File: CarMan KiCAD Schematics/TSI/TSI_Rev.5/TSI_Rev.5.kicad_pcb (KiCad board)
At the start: 2 copper layers, 203.2 x 165.1 mm, 259 parts, among them IC1 TS431ILT, IC4 TS431ILT, J1 J1, J10 J10, J11 J11, J12 J12, J13 Conn_01x01, J13.1 Conn_01x06, J13.2 Conn_01x06, J14 J14, J15 J15, J16 J16, J17 J17, J18 J18, J19 J19, J2 Current_Sensor, J20 J20, J21 J21, J22 J22, J23 J23, J24 Conn_01x01, J25 Conn_01x01, J26 J26, J27 J27, J28 Conn_01x01, J29 J29, J3 J3, J30 J23, J4 J4, J5 J5, J6 J6, J7 J7, J8 J8, J9 J9, K1 APAN3105, K2 G5LE-1-E, K3 SFS2-DC24V, K4 SFS2-DC24V, Q1 ZVP1320F, Q11 TN2130K1-G, Q2 MMBF170, Q3 ZVP1320F, Q5 SI1302DL-T1-E3, SW1 TS5A3159DBVT, U1 RDE03110S12, U10 MC7805BDTRKG, U11 TLP293, U12 REF3033, U13 TLP293, U14 Bottom Left, U15 Top Left, U16 TS372CDT, U17 Top Right, U18 MCP6004, U19 74HC00, U2 Bottom Right, U20 TLP293, U21 MCP6004, U22 MCP23016-I_SO, U23 DAC5574IDGS, U24 TLP293, U25 NCD9830DBR2G, U26 MCP6004, U29 SN74LVC1G08DCKR, U3 TS912, U30 TLP293, U31 TLP293, U32 TLP293, U34 TLP293, U35 MCP6004, U37 TLP293, U4 ACPL-C870, U40 MCP6004, U41 PDQ10-Q24-D5-D, U42 LT1763CS8-3.3PBF, U48 TLP293, U49 TLP293, U5 SI8600AB-B-IS, U6 TS912, U7 MCP6004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

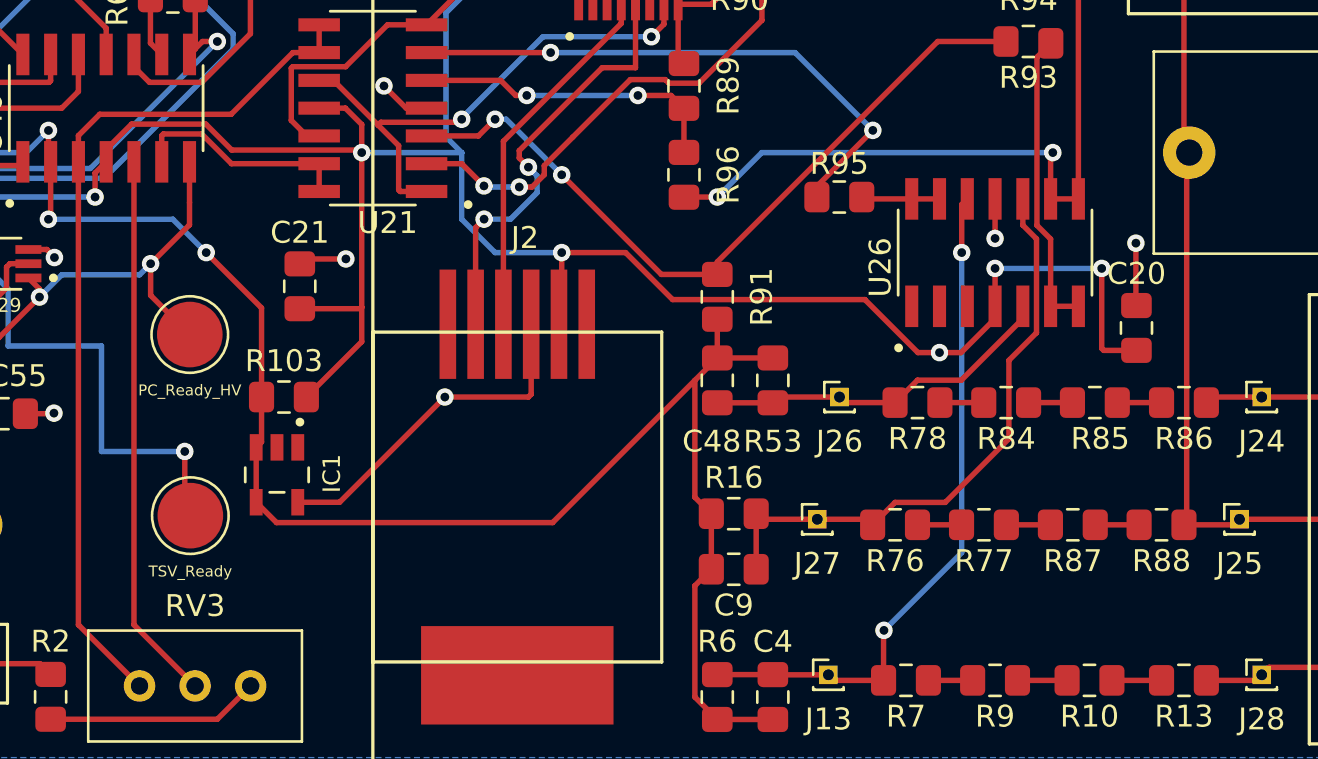
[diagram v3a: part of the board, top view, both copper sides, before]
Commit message: Contemplated homicide and fixed PC schematic
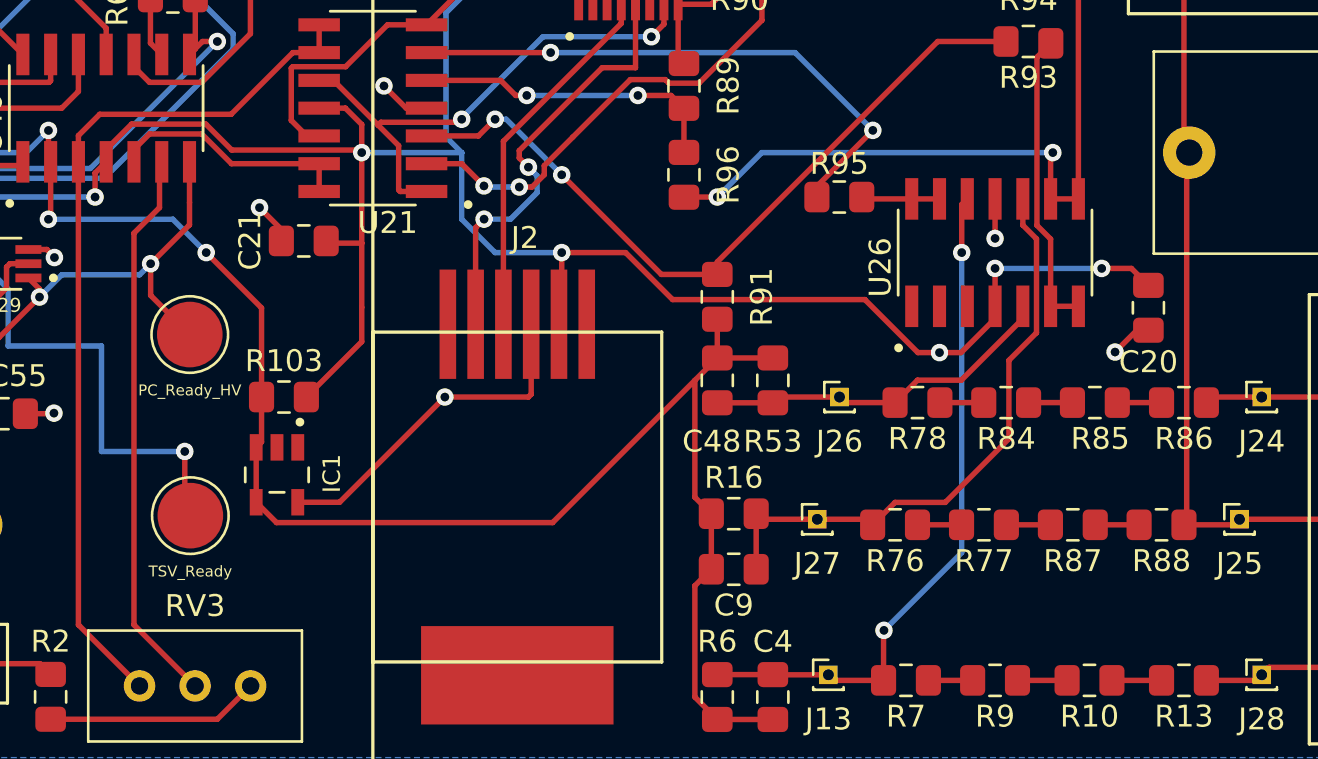
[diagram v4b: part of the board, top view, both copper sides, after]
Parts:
- moved C21 2.08 mm to (230.1, 194.1), turned to 180 degrees
- moved C20 1.07 mm to (268.7, 197.1), turned to 270 degrees
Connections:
- U40 pad 5: Net-(RV3-Pad2) -> Net-(U21-Pad13)
- U40 pad 6: Net-(U21-Pad13) -> Net-(RV3-Pad2)
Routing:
- net /5HV: track 312.8 -> 308.8 mm
- net /DC_RELAY-: track 100.9 -> 99.7 mm
- net Net-(U21-Pad13): track 10.3 -> 11.2 mm
- net Net-(RV3-Pad2): track 25.1 -> 25.6 mm

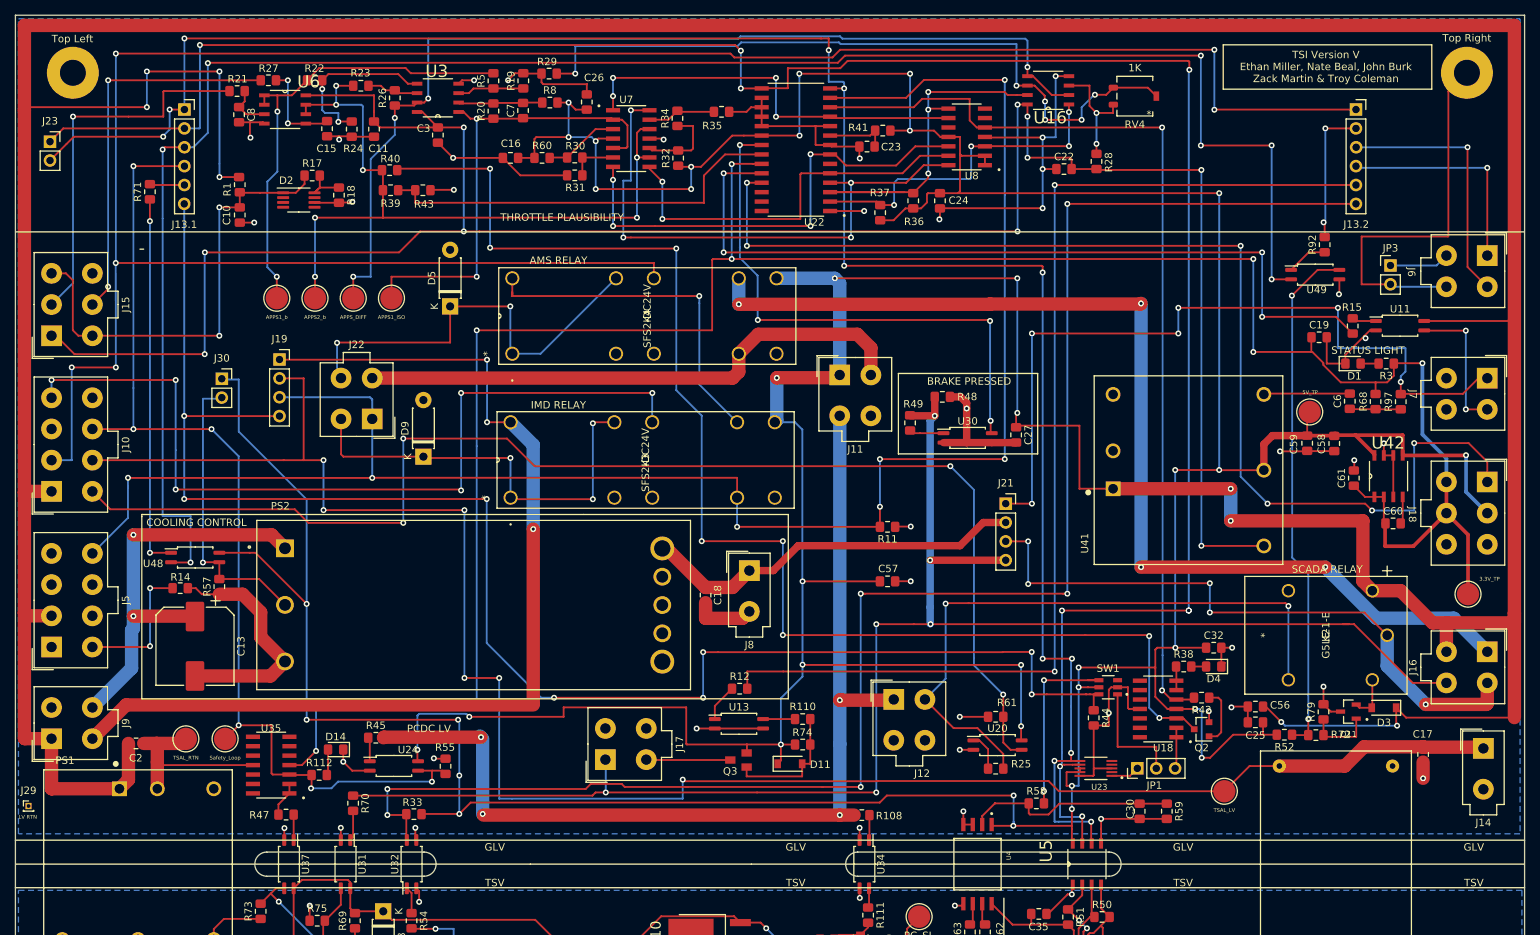
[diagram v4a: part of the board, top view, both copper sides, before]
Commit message: - Increased spacing between edge cuts and 24V - Labeled more in Low voltage
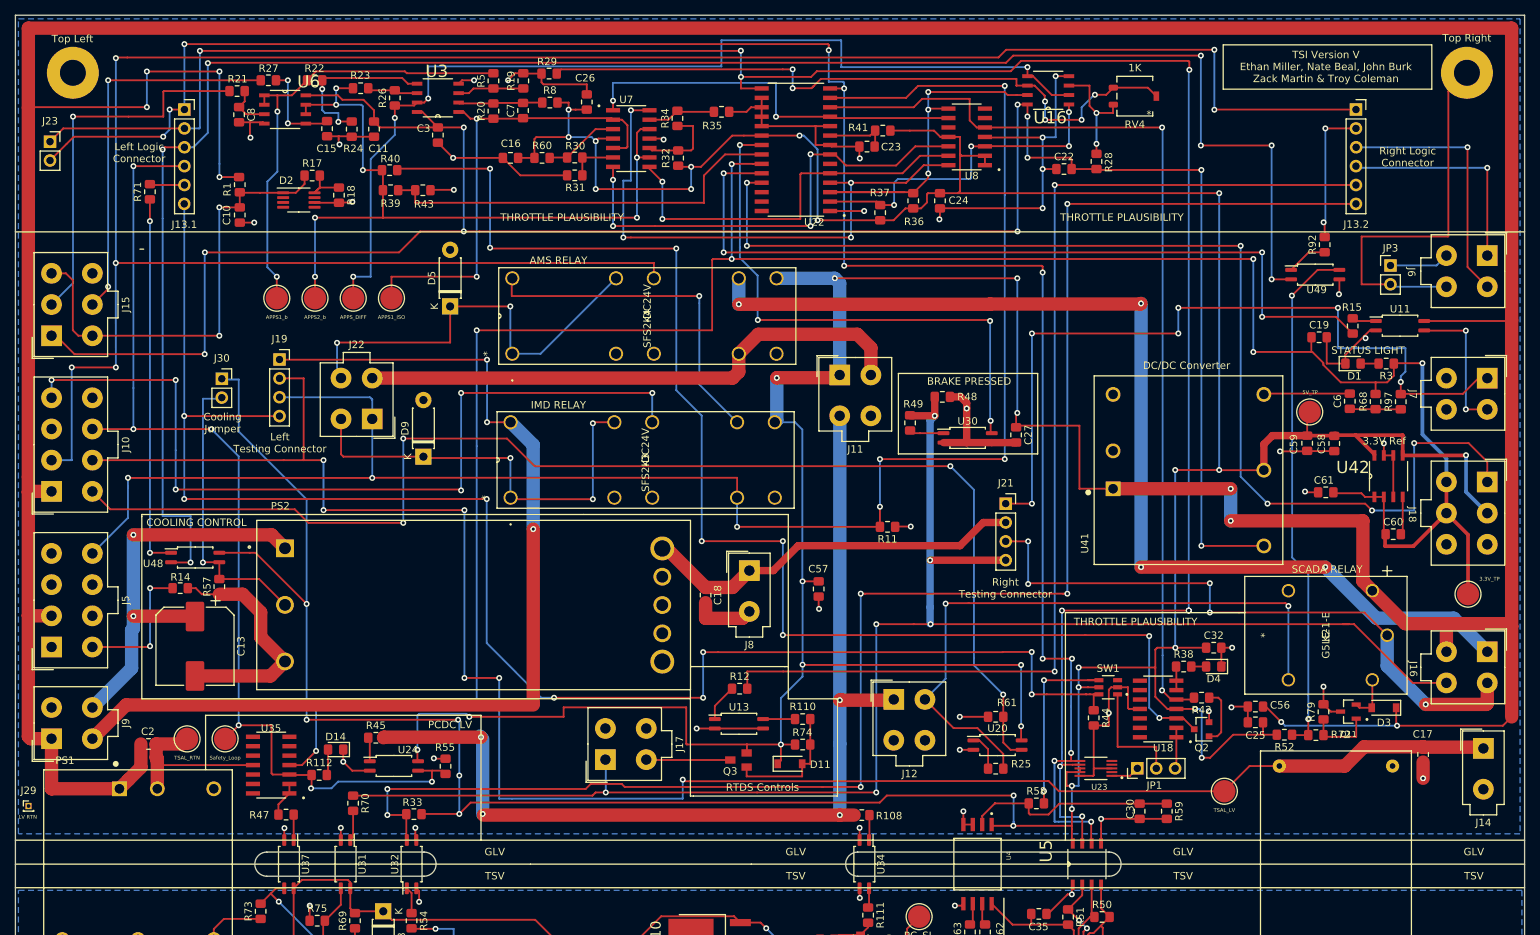
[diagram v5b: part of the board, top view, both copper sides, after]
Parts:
- moved C57 9.33 mm to (208.3, 130.1), turned to 270 degrees
- moved C61 4.24 mm to (276.6, 117.1), turned to 180 degrees
- moved C2 1.68 mm to (118.1, 151.0)
- moved C60 1.45 mm to (285.7, 122.7)
- moved R23 0.33 mm to (146.7, 62.7)
- moved TP14 0.17 mm to (123.3, 150.3)
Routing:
- net /24V: track 864.3 -> 850.7 mm
- net /5V: track 569.4 -> 559.3 mm, vias 28 -> 26
- net Net-(R29-Pad1): track 97.4 -> 92.2 mm
- net /3.3V: track 311.4 -> 313.8 mm
- net Net-(C60-Pad2): track 3.68 -> 5.28 mm
- net /SCL: track 270.3 -> 268.7 mm
- net /TSI-TP/U8_Pin9: track 54.8 -> 53.5 mm, vias 4 -> 2
- net /10V: track 298.4 -> 297.2 mm
- net /IMD_Status: track 245.1 -> 244.0 mm
- net /AIRS-: track 361.0 -> 360.0 mm
- net /AMS_FAULT_LED: track 313.5 -> 313.0 mm
- net /TSI-TP/APPS_DIFF: track 135.0 -> 134.5 mm
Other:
- board text added: "3.3V Ref"
- board text added: "Cooling Jumper"
- board text added: "DC/DC Converter"
- board text added: "J16"
- board text added: "Left Logic Connector"
- board text added: "Left Testing Connector"
- board text added: "RTDS Controls"
- board text added: "Right Logic Connector"
- board text added: "Right Testing Connector"

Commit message: TSI Silkscreen Connector Descriptions added
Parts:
- J1 HV: renamed from J1
- J10 DASH: renamed from J10
- J11 BP PWR: renamed from J11
- J12 MRST SLOOP: renamed from J12
- J13.1 Logic: renamed from J13.1
- J13.2 Logic: renamed from J13.2
- J14 TSAL: renamed from J14
- J15 Throt. Plaus.: renamed from J15
- J17 Light RTDS: renamed from J17
- J2 Current: renamed from J2
- J20 Discharge : renamed from J20
- J22 LSP: renamed from J22
- J23 I2C: renamed from J23
- J3 PC: renamed from J3
- J4 MC: renamed from J4
- J5 IMD: renamed from J5
- J8 COOL PWR: renamed from J8
- J9 GLV: renamed from J9
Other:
- board text added: "J16 Brake"
- board text added: "J18 COOL Sensor"
- board text added: "J6 BP CAN"
- board text added: "J7 Cockpit"
- board text removed: "J16"
- board text removed: "J18"
- board text removed: "J6"
- board text removed: "J7"

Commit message: TSI silkscreen updated
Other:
- board text added: "TSI Version V Nate Beal, Ethan Miller, John Burk Zack Martin & Troy Coleman"
- board text removed: "TSI Version V Ethan Miller, Nate Beal, John Burk Zack Martin & Troy Coleman"
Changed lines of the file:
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@@
   (general
     (thickness 1.6)
-    (drawings 89)
+    (drawings 88)
     (tracks 2617)
     (zones 0)
@@
     (descr "Molex Mini-Fit JR, PN:5556-04A, dual row, top entry type, through hole")
     (tags "connector molex mini-fit 5556")
-    (fp_text reference "J9 GLV" (at -0.2286 9.8933 90) (layer F.SilkS)
+    (fp_text reference "J9 GLV" (at 1.8288 10.1219 90) (layer F.SilkS)
       (effects (font (size 1 1) (thickness 0.15)))
     )
@@
     (descr "Molex Mini-Fit JR, PN:5556-08A, dual row, top entry type, through hole")
     (tags "connector molex mini-fit 5556")
-    (fp_text reference "J5 IMD" (at 7.747 10 90) (layer F.SilkS)
+    (fp_text reference "J5 IMD" (at 6.2484 10.1219 90) (layer F.SilkS)
       (effects (font (size 1 1) (thickness 0.15)))
     )
@@
     (effects (font (size 1 1) (thickness 0.15)))
   )
-  (gr_text "TSI Version V\nEthan Miller, Nate Beal, John Burk\nZack Martin & Troy Coleman" (at 276.6187 59.7916) (layer F.SilkS)
+  (gr_text "TSI Version V\nNate Beal, Ethan Miller, John Burk\nZack Martin & Troy Coleman" (at 276.6187 59.7916) (layer F.SilkS)
     (effects (font (size 1 1) (thickness 0.15)))
   )
@@
     (effects (font (size 1 1) (thickness 0.15)))
   )
-  (gr_line (start 117.4496 84.3534) (end 116.9416 84.3534) (layer F.SilkS) (width 0.15))
   (gr_line (start 233.2736 171.7294) (end 233.2736 217.9574) (layer F.SilkS) (width 0.15))
   (gr_arc (start 155.194 167.1574) (end 155.194 168.783) (angle -180) (layer Edge.Cuts) (width 0.1))

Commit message: TSI
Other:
- board text added: "TSI Version V Ethan Miller, Nate Beal, John Burk Zack Martin & Troy Coleman"
- board text removed: "TSI Version V Nate Beal, Ethan Miller, John Burk Zack Martin & Troy Coleman"
